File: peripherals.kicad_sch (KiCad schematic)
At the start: 93 parts, among them J10 Molex_PicoBlade_1x4_0533980471, J11 Socket_Samtec_ERF8_2x40_ERF8-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, J14 JST_SH_1x4_SM04B-SRSS-TB-LF-SN, J9 Tag-Connect_TC2050-IDC-NL_2x5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, Q10 PJE138K, Q9 PJE138K, U30 TPD4E05U06QDQARQ1, U33 NTS0102_XSON, U34 PCAL6408A_VQFN, U35 AP22653_DFN

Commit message: Init commit
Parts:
- C104, C111, C113, C130, C44, C48: LCSC Part # (none) -> C85960
- C105, C106, C107, C114, C115: LCSC Part # (none) -> C2182694
- C108, C109, C110, C112: LCSC Part # (none) -> C106257
- D16, D17, D19, D21, D22, D23, D39, D40, D41, D42, D43, D44, D45, D46, D47, D48, D49, D50, D56, D57, D58, D59: LCSC Part # (none) -> C5182093
- D26, D27, D54: LCSC Part # (none) -> C125093
- D63: LCSC Part # (none) -> C145179
- J10: LCSC Part # (none) -> C234195
- J11: LCSC Part # (none) -> C3649331
- J14: LCSC Part # (none) -> C160404
- J9: LCSC Part # (none) -> C4371149
- Q10, Q9: LCSC Part # (none) -> C391643
- R100, R101, R102, R26, R53, R54, R63, R64: LCSC Part # (none) -> C2654089
- R112: LCSC Part # (none) -> C178752
- R120, R121, R134, R141, R215, R216, R217, R218, R55, R62: LCSC Part # (none) -> C242160
- R189, R219, R232, R242: LCSC Part # (none) -> C202396
- R190: LCSC Part # (none) -> C19946417
- R191, R223, R231: LCSC Part # (none) -> C19946422
- R192, R222, R230: LCSC Part # (none) -> C2077080
- R195, R204, R25: LCSC Part # (none) -> C1731295
- R233, R235, R248: LCSC Part # (none) -> C253507
- R234, R247: LCSC Part # (none) -> C512908
- R335, R336: LCSC Part # (none) -> C2077077
- S2, S3: LCSC Part # (none) -> C221676
- U30: LCSC Part # (none) -> C81353
- U33: LCSC Part # (none) -> C2687851
- U34: LCSC Part # (none) -> C2652332
- U35: LCSC Part # (none) -> C3001604

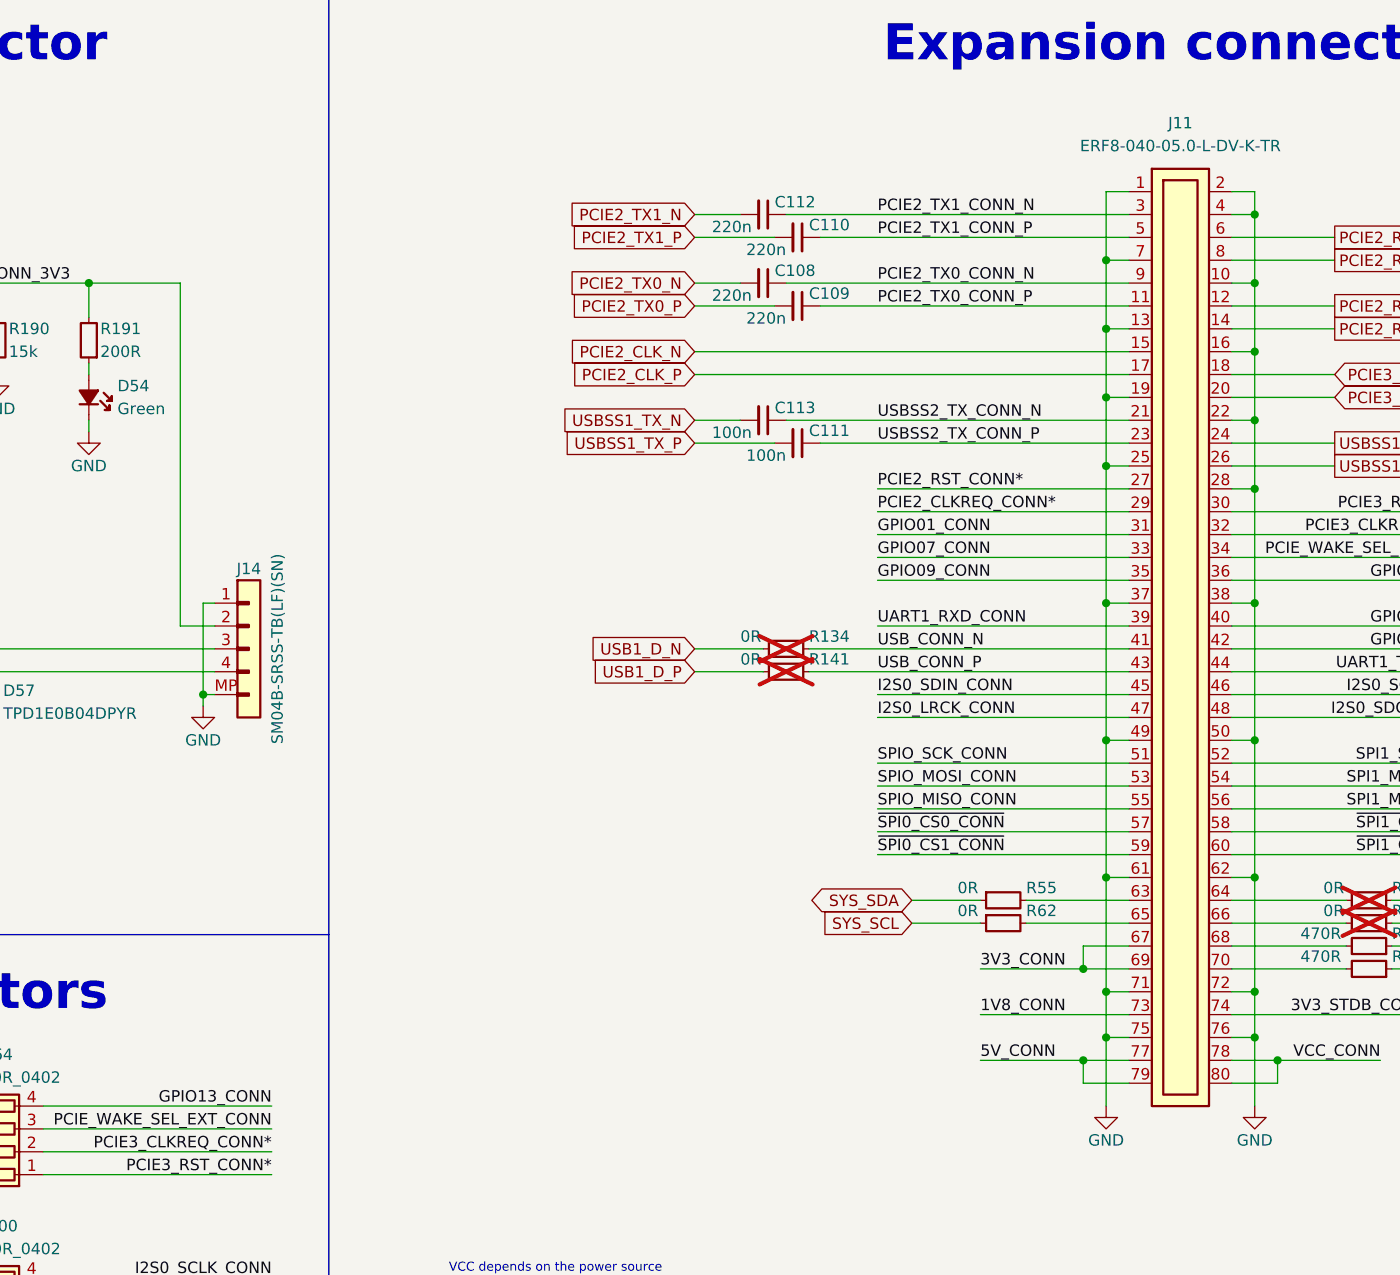
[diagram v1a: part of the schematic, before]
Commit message: Add field Digikey Part Number. Add Chinese substitute components
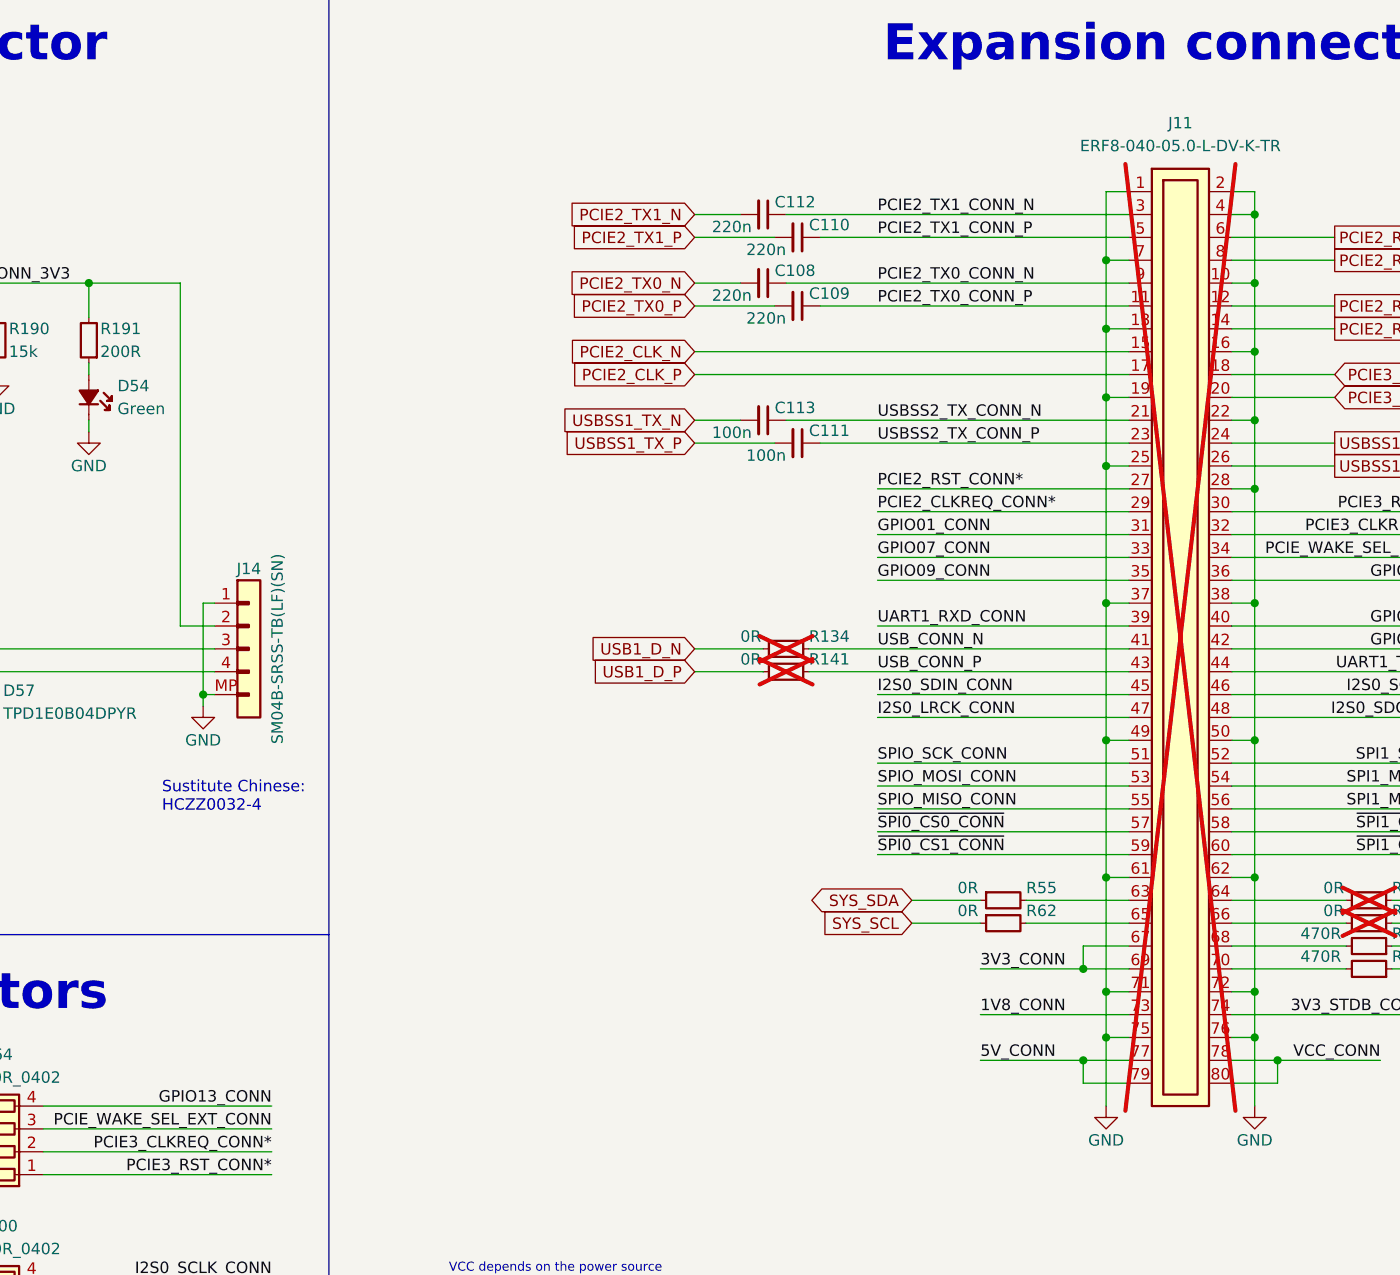
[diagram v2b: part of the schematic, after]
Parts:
- C104, C111, C113, C130, C44, C48: Digikey Part # (none) -> 490-10697-1-ND
- C105, C106, C107, C114, C115: Alternative MPN (none) -> CL05A105KA5NQNC; Digikey Part # (none) -> 445-7368-1-ND
- C108, C109, C110, C112: Digikey Part # (none) -> 311-1421-1-ND
- D16, D17, D19, D21, D22, D23, D39, D40, D41, D42, D43, D44, D45, D46, D47, D48, D49, D50, D56, D57, D58, D59: Digikey Part # (none) -> 296-47864-1-ND
- D26, D27, D54: Alternative MPN (none) -> LTST-C190KRKT; Digikey Part # (none) -> 160-1183-1-ND
- D63: Digikey Part # (none) -> RB521S30T1GOSCT-ND
- J10: Digikey Part # (none) -> WM7608CT-ND
- J11: Digikey Part # (none) -> SAM13136CT-ND; now not fitted; now left out of the parts list
- J14: Digikey Part # (none) -> 455-SM04B-SRSS-TBCT-ND
- J9: Digikey Part # (none) -> TC2050-IDC-NL-ND
- Q10, Q9: Digikey Part # (none) -> 3757-PJE138K_R1_00001CT-ND
- R100, R101, R102, R26, R53, R54, R63, R64: Digikey Part # (none) -> Y7331CT-ND
- R112: Digikey Part # (none) -> Y6101CT-ND
- R120, R121, R134, R141, R215, R216, R217, R218, R55, R62: Digikey Part # (none) -> P0.0JCT-ND
- R189, R219, R232, R242: Digikey Part # (none) -> CR0402-FX-1002GLFCT-ND
- R190: Digikey Part # (none) -> CR0402-FX-1502GLFCT-ND
- R191, R223, R231: Digikey Part # (none) -> CR0402-FX-2000GLFCT-ND
- R192, R222, R230: Digikey Part # (none) -> CR0402-FX-1003GLFCT-ND
- R195, R204, R25: Digikey Part # (none) -> Y6000CT-ND
- R233, R235, R248: Digikey Part # (none) -> 846-PMR03EZPJ000CT-ND
- R234, R247: Digikey Part # (none) -> CR0603-J/-000ELFCT-ND
- R335, R336: Digikey Part # (none) -> CR0402-FX-4700GLFCT-ND
- S2, S3: Digikey Part # (none) -> CKN10243CT-ND
- U30: Digikey Part # (none) -> 296-40696-1-ND
- U33: Digikey Part # (none) -> 568-5205-1-ND
- U34: Digikey Part # (none) -> 568-11578-1-ND
- U35: Digikey Part # (none) -> 31-AP22653FDZ-7CT-ND
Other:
- note added: "Sustitute Chinese: HCZZ0032-4"
